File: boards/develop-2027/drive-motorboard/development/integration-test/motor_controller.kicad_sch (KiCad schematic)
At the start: 28 parts, among them U6 STSPIN32G0A2

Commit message: reformat root sheet, assign parts numbers for generics
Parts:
- C10: renamed from C14; footprint Capacitor_SMD:C_0402_1005Metric -> Capacitor_SMD:C_0603_1608Metric; Manufacturer P/N (none) -> GRM188D72A105KE01J; Vendor (none) -> DigiKey; Vendor P/N (none) -> 490-GRM188D72A105KE01JCT-ND
- C11: renamed from C15; Manufacturer P/N (none) -> GRM155R71H272KA01J; Vendor (none) -> DigiKey; Vendor P/N (none) -> 490-6361-1-ND
- C12: renamed from C16; footprint Capacitor_SMD:C_0402_1005Metric -> Capacitor_SMD:C_0603_1608Metric; Manufacturer P/N (none) -> GRM188D72A105KE01J; Vendor (none) -> DigiKey; Vendor P/N (none) -> 490-GRM188D72A105KE01JCT-ND
- C13: renamed from C17; footprint Capacitor_SMD:C_0402_1005Metric -> Capacitor_SMD:C_0603_1608Metric; Manufacturer P/N (none) -> GRM188D72A105KE01J; Vendor (none) -> DigiKey; Vendor P/N (none) -> 490-GRM188D72A105KE01JCT-ND
- C5: renamed from C9; footprint Capacitor_SMD:C_0805_2012Metric -> Capacitor_SMD:C_0603_1608Metric; Manufacturer P/N (none) -> GRM188D72A105KE01J; Vendor (none) -> DigiKey; Vendor P/N (none) -> 490-GRM188D72A105KE01JCT-ND
- C6: renamed from C10; Manufacturer P/N (none) -> GRM155R61E105KA12D; Vendor (none) -> DigiKey; Vendor P/N (none) -> 490-10017-1-ND
- C7: renamed from C11; Manufacturer P/N (none) -> CL05A104KA5NNNC; Vendor (none) -> DigiKey; Vendor P/N (none) -> 1276-1043-1-ND
- C8: renamed from C12; Manufacturer P/N (none) -> GRM188R6YA106MA73D; Vendor (none) -> DigiKey; Vendor P/N (none) -> 490-13248-1-ND
- C9: renamed from C13; Manufacturer P/N (none) -> CL05A104KA5NNNC; Vendor (none) -> DigiKey; Vendor P/N (none) -> 1276-1043-1-ND
- D3: renamed from D9; Manufacturer P/N (none) -> LTST-C190KRKT; Vendor (none) -> DigiKey; Vendor P/N (none) -> 160-1436-1-ND
- R12: renamed from R21; Manufacturer P/N (none) -> RC0402FR-074K7L; Vendor (none) -> DigiKey; Vendor P/N (none) -> 311-4.7KLRCT-ND
- TP10: renamed from TP19; Manufacturer P/N (none) -> 5002; Vendor (none) -> DigiKey; Vendor P/N (none) -> 36-5002-ND
- TP11: renamed from TP20; Manufacturer P/N (none) -> 5002; Vendor (none) -> DigiKey; Vendor P/N (none) -> 36-5002-ND
- TP12: renamed from TP21; Manufacturer P/N (none) -> 5002; Vendor (none) -> DigiKey; Vendor P/N (none) -> 36-5002-ND
- TP13: renamed from TP22; Manufacturer P/N (none) -> 5002; Vendor (none) -> DigiKey; Vendor P/N (none) -> 36-5002-ND
- TP4: renamed from TP13; Manufacturer P/N (none) -> 5000; Vendor (none) -> DigiKey; Vendor P/N (none) -> 36-5000-ND
- TP5: renamed from TP14; Manufacturer P/N (none) -> 5000; Vendor (none) -> DigiKey; Vendor P/N (none) -> 36-5000-ND
- TP6: renamed from TP15; Manufacturer P/N (none) -> 5000; Vendor (none) -> DigiKey; Vendor P/N (none) -> 36-5000-ND
- TP7: renamed from TP16; Manufacturer P/N (none) -> 5002; Vendor (none) -> DigiKey; Vendor P/N (none) -> 36-5002-ND
- TP8: renamed from TP17; Manufacturer P/N (none) -> 5002; Vendor (none) -> DigiKey; Vendor P/N (none) -> 36-5002-ND
- TP9: renamed from TP18; Manufacturer P/N (none) -> 5002; Vendor (none) -> DigiKey; Vendor P/N (none) -> 36-5002-ND
- renumbered C7 to C3, C8 to C4, R22 to R13, R23 to R14, R24 to R15, R25 to R16, U6 to U1

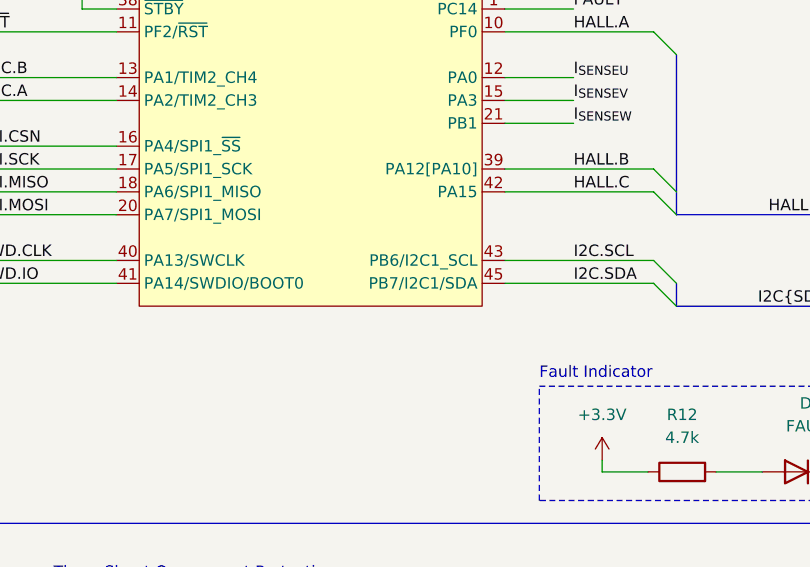
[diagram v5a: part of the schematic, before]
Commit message: Set up PCB design rules
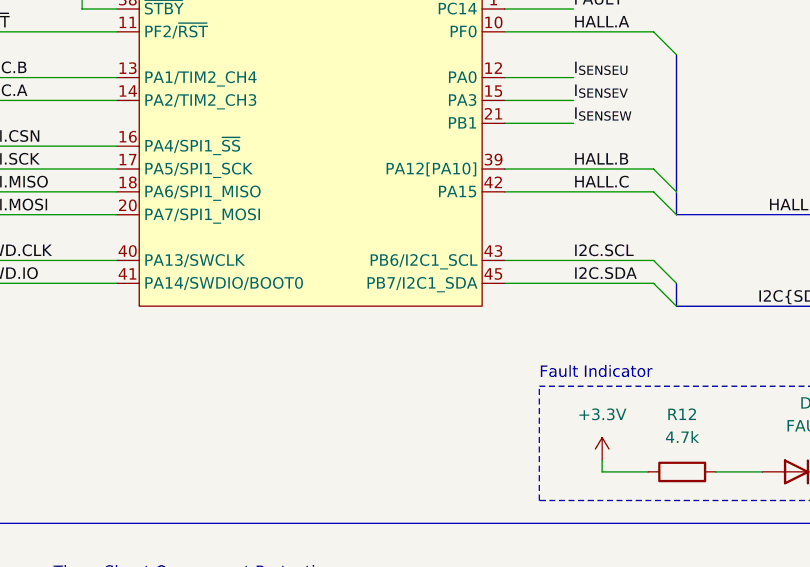
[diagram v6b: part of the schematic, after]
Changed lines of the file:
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@@
 			)
 		)
-		(property "Description" "1 µF ±10% 100V Ceramic Capacitor X7T 0603 (1608 Metric)"
+		(property "Description" "Unpolarized capacitor"
 			(at 44.45 179.07 0)
 			(hide yes)
@@
 			)
 		)
-		(property "Description" "White PC Test Point, Miniature Phosphor Bronze Silver Plating Through Hole Mounting Type"
+		(property "Description" "test point"
 			(at 66.675 179.705 0)
 			(hide yes)
@@
 			)
 		)
-		(property "Description" "White PC Test Point, Miniature Phosphor Bronze Silver Plating Through Hole Mounting Type"
+		(property "Description" "test point"
 			(at 66.675 150.495 0)
 			(hide yes)
@@
 			)
 		)
-		(property "Description" "1 µF ±10% 100V Ceramic Capacitor X7T 0603 (1608 Metric)"
+		(property "Description" "Unpolarized capacitor"
 			(at 62.23 38.1 0)
 			(hide yes)
@@
 			)
 		)
-		(property "Description" "White PC Test Point, Miniature Phosphor Bronze Silver Plating Through Hole Mounting Type"
+		(property "Description" "test point"
 			(at 66.675 121.285 0)
 			(hide yes)
@@
 			)
 		)
-		(property "Description" "100 µF 35 V Aluminum Electrolytic Capacitors Radial, Can - SMD 260mOhm @ 100kHz 2000 Hrs @ 105°C"
+		(property "Description" "Polarized capacitor"
 			(at 48.26 38.1 0)
 			(hide yes)
@@
 			)
 		)
-		(property "Description" "5.62 kOhms ±0.1% 1/16W Chip Resistor 0402 (1005 Metric) Thin Film ±25ppm/°C"
+		(property "Description" "Resistor"
 			(at 222.25 114.3 0)
 			(hide yes)
@@
 			)
 		)
-		(property "Description" "Red PC Test Point, Miniature Phosphor Bronze Silver Plating Through Hole Mounting Type"
+		(property "Description" "test point"
 			(at 107.95 73.66 0)
 			(hide yes)
@@
 			)
 		)
-		(property "Description" "100 µF 35 V Aluminum Electrolytic Capacitors Radial, Can - SMD 260mOhm @ 100kHz 2000 Hrs @ 105°C"
+		(property "Description" "Polarized capacitor"
 			(at 31.75 38.1 0)
 			(hide yes)
@@
 			)
 		)
-		(property "Description" "1.13 kOhms ±0.1% 1/16W Chip Resistor 0402 (1005 Metric) Thin Film ±25ppm/°C"
+		(property "Description" "Resistor"
 			(at 203.2 133.35 0)
 			(hide yes)
@@
 			)
 		)
-		(property "Description" "Red PC Test Point, Miniature Phosphor Bronze Silver Plating Through Hole Mounting Type"
+		(property "Description" "test point"
 			(at 62.23 30.48 0)
 			(hide yes)
@@
 			)
 		)
-		(property "Description" "White PC Test Point, Miniature Phosphor Bronze Silver Plating Through Hole Mounting Type"
+		(property "Description" "test point"
 			(at 241.3 114.3 0)
 			(hide yes)
@@
 			)
 		)
-		(property "Description" "1.13 kOhms ±0.1% 1/16W Chip Resistor 0402 (1005 Metric) Thin Film ±25ppm/°C"
+		(property "Description" "Resistor"
 			(at 203.2 107.95 0)
 			(hide yes)
@@
 			)
 		)
-		(property "Description" "Red PC Test Point, Miniature Phosphor Bronze Silver Plating Through Hole Mounting Type"
+		(property "Description" "test point"
 			(at 50.8 55.88 0)
 			(hide yes)
@@
 			)
 		)
-		(property "Description" "White PC Test Point, Miniature Phosphor Bronze Silver Plating Through Hole Mounting Type"
+		(property "Description" "test point"
 			(at 57.15 121.285 0)
 			(hide yes)
@@
 			)
 		)
-		(property "Description" "White PC Test Point, Miniature Phosphor Bronze Silver Plating Through Hole Mounting Type"
+		(property "Description" "test point"
 			(at 57.15 179.705 0)
 			(hide yes)
@@
 			)
 		)
-		(property "Description" "White PC Test Point, Miniature Phosphor Bronze Silver Plating Through Hole Mounting Type"
+		(property "Description" "test point"
 			(at 57.15 150.495 0)
 			(hide yes)
@@
 			)
 		)
-		(property "Description" "1.13 kOhms ±0.1% 1/16W Chip Resistor 0402 (1005 Metric) Thin Film ±25ppm/°C"
+		(property "Description" "Resistor"
 			(at 203.2 120.65 0)
 			(hide yes)
@@
 			)
 		)
-		(property "Description" "1 µF ±10% 100V Ceramic Capacitor X7T 0603 (1608 Metric)"
+		(property "Description" "Unpolarized capacitor"
 			(at 44.45 149.86 0)
 			(hide yes)
@@
 			)
 		)
-		(property "Description" "1 µF ±10% 100V Ceramic Capacitor X7T 0603 (1608 Metric)"
+		(property "Description" "Unpolarized capacitor"
 			(at 44.45 120.65 0)
 			(hide yes)
